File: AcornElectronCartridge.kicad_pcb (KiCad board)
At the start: 2 copper layers, 84.9 x 62.5 mm, 8 parts, among them P11 CONN_01X08, P12 CONN_01X08, P13 CONN_01X06, P21 CONN_01X06, P22 CONN_01X08, P23 CONN_01X08

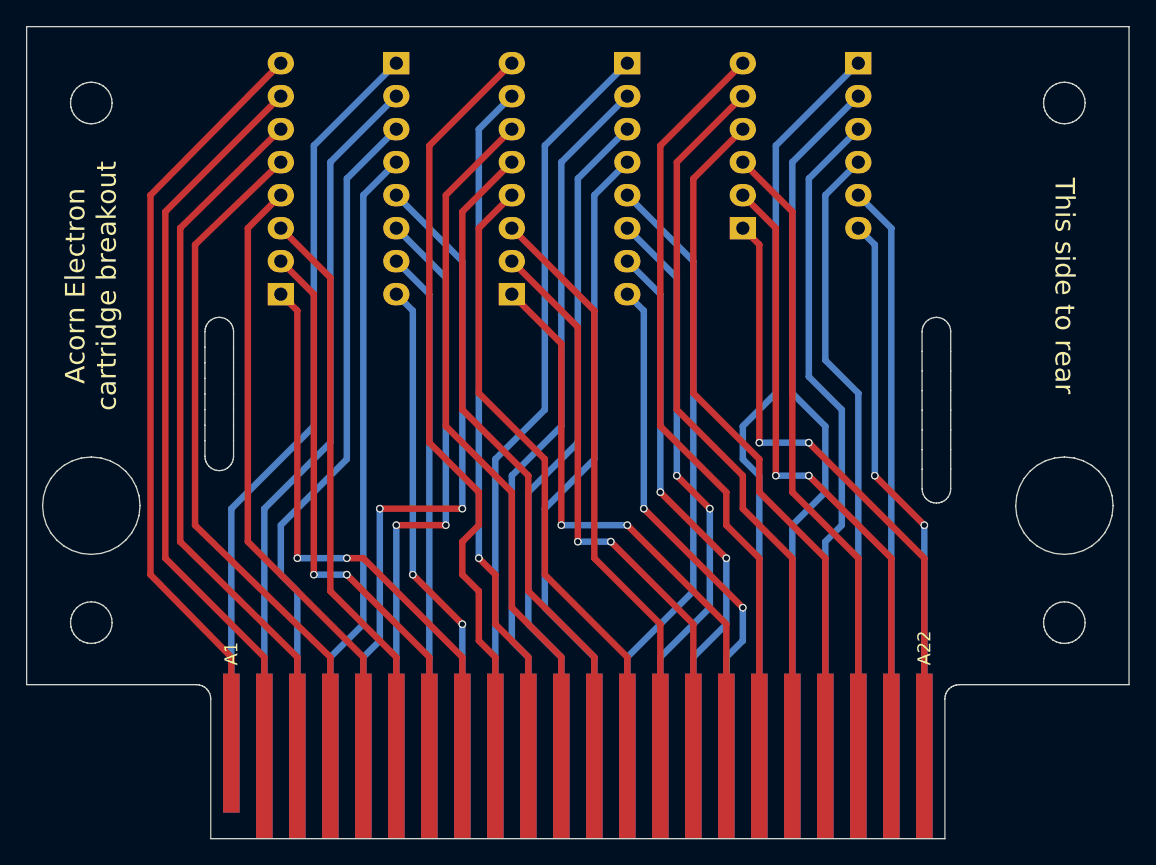
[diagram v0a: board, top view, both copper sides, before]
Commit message: Removed footprints, pads, vias and tracks. Changed labels to reflect the new use for the design.
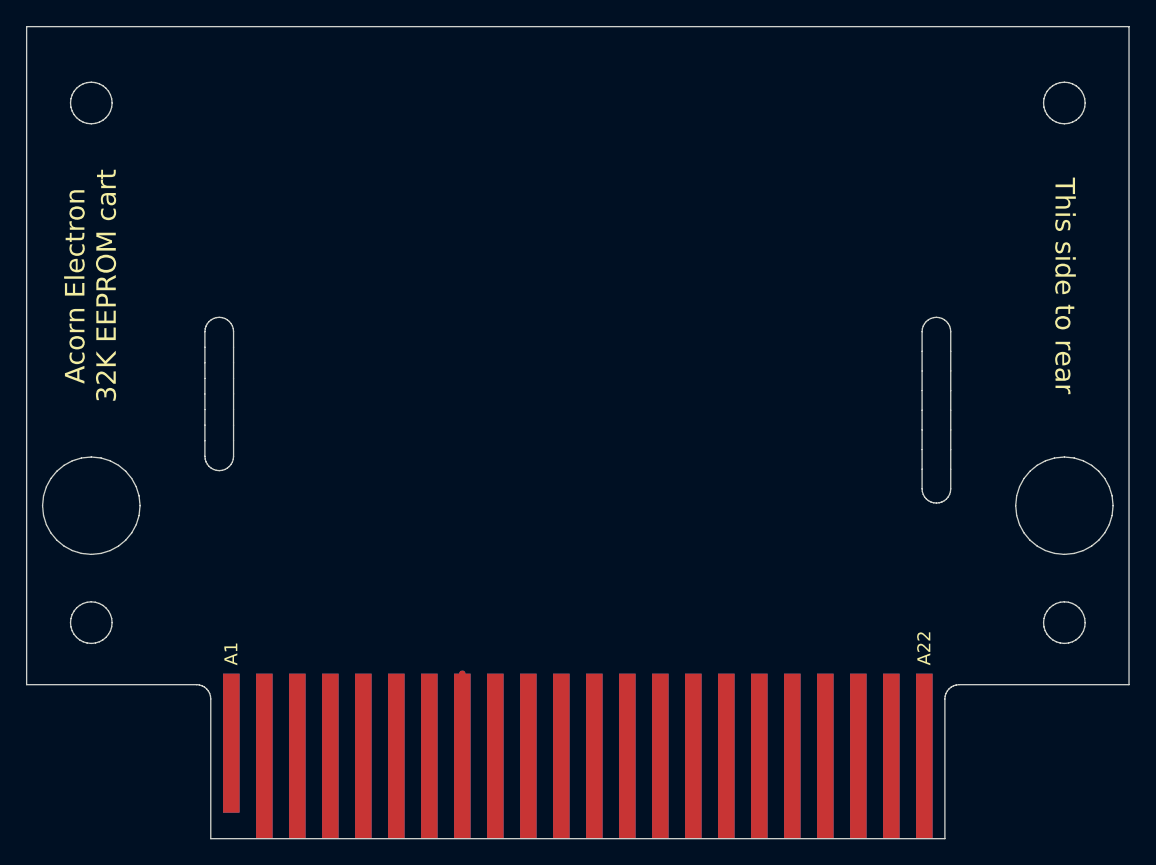
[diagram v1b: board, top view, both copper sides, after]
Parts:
- removed P11, P12, P22, P23: CONN_01X08, Pin_Headers:Pin_Header_Straight_1x08
- removed P13, P21: CONN_01X06, Pin_Headers:Pin_Header_Straight_1x06
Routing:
- net /+5V_A: track 60.0 -> 0.00 mm
- net /CLOCK: track 59.1 -> 0.00 mm
- net /-5V: track 59.1 -> 0.00 mm
- net /+5V_B: track 58.6 -> 0.00 mm
- net /nOE: track 57.6 -> 0.00 mm
- net /D4: track 57.5 -> 0.00 mm
- net /BA1: track 57.5 -> 0.00 mm
- net /nROMSTB: track 56.6 -> 0.00 mm
- net /nRST: track 55.3 -> 0.00 mm
- net /A10: track 55.0 -> 0.00 mm
- net /nOE2: track 55.0 -> 0.00 mm
- net /BA0: track 55.0 -> 0.00 mm
- net /READY: track 54.0 -> 0.00 mm
- net /ADOUT: track 54.0 -> 0.00 mm
- net /NC: track 53.4 -> 0.00 mm, vias 1 -> 0
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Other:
- board text added: "(C) 2017 David Boddie <david@boddie.org.uk> Design licensed under GPLv3 or later"
- board text added: "Acorn Electron 32K EEPROM cart"
- board text removed: "+5V"
- board text removed: "-5V"
- board text removed: "0V"
- board text removed: "A10"
- board text removed: "A11"
- board text removed: "A12"
- board text removed: "A13"
- board text removed: "A8"
- board text removed: "A9"
- board text removed: "ADIN"
- board text removed: "ADOUT"
- board text removed: "AGND"
- board text removed: "BA0"
- board text removed: "BA1"
- board text removed: "BA2"
- board text removed: "BA3"
- board text removed: "BA4"
- board text removed: "BA5"
- board text removed: "BA6"
- board text removed: "BA7"
- board text removed: "CLOCK"
- board text removed: "CSRW"
- board text removed: "Copyright (C) 2017 Paul Boddie <paul@boddie.org.uk> Design licensed under GPLv3 or later"
- board text removed: "D0"
- board text removed: "D1"
- board text removed: "D2"
- board text removed: "D3"
- board text removed: "D4"
- board text removed: "D5"
- board text removed: "D6"
- board text removed: "D7"
- board text removed: "NC"
- board text removed: "PHI2"
- board text removed: "READY"
- board text removed: "ROMQA"
- board text removed: "nINFC"
- board text removed: "nINFD"
- board text removed: "nIRQ"
- board text removed: "nNMI"
- board text removed: "nOE"
- board text removed: "nOE2"
- board text removed: "nROMSTB"
- board text removed: "nRST"

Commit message: Finished the basic design.
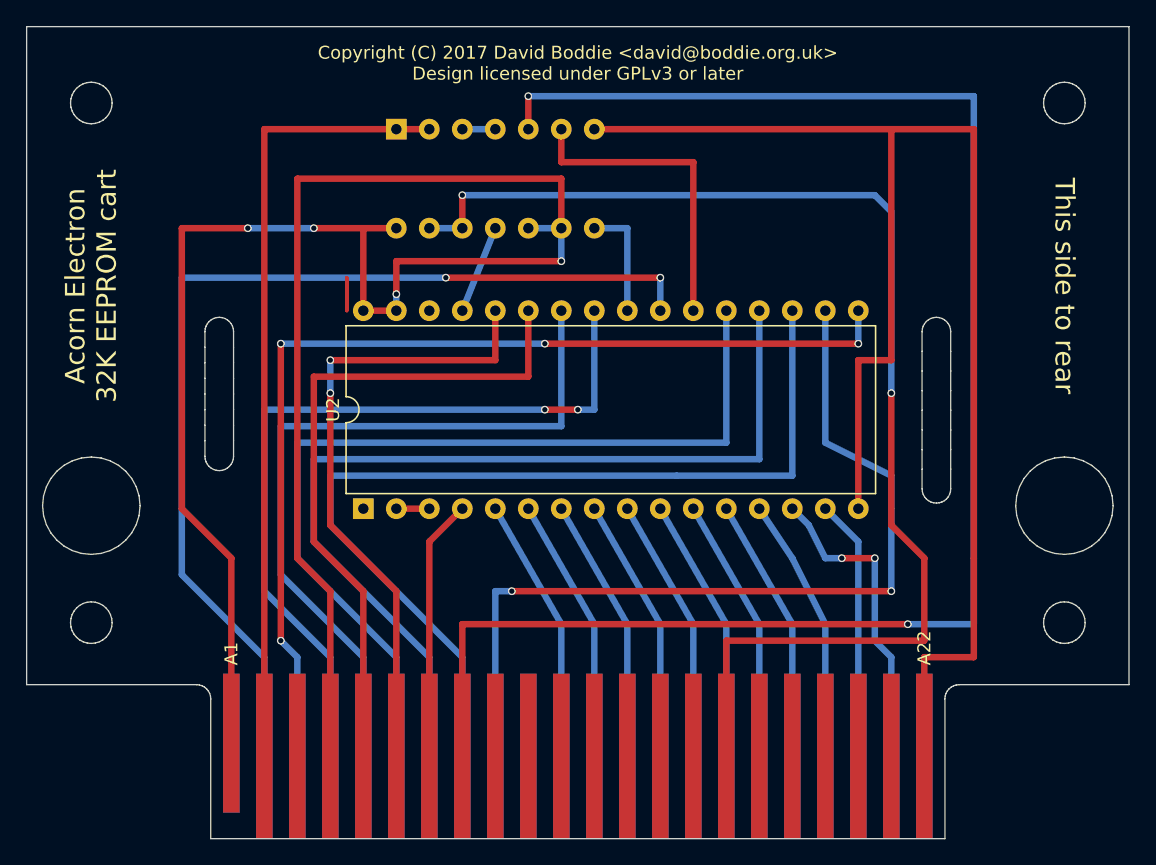
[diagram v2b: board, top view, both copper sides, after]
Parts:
- added U1: 74HC00, Housings_DIP:DIP-14_W7.62mm, B.Cu at (88.9, 72.4)
- added U2: SST39SF010, Housings_DIP:DIP-32_W15.24mm, F.Cu at (86.4, 101.6)
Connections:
- CONN1 pad 1: /+5V_A -> VCC
- CONN1 pad 22: /0V_A -> GND
- CONN2 pad 22: /0V_B -> GND
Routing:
- net /PHI2: track 6.35 -> 127.0 mm, vias 0 -> 2
- net GND: track 0.00 -> 115.6 mm
- net /ROMQA: track 0.00 -> 96.8 mm, vias 0 -> 2
- net /CSRW: track 0.00 -> 91.2 mm, vias 0 -> 2
- net /D3: track 0.00 -> 79.3 mm, vias 0 -> 4
- net /A10: track 0.00 -> 78.8 mm, vias 0 -> 2
- net /D5: track 0.00 -> 74.1 mm
- net /D6: track 0.00 -> 72.3 mm
- net /D7: track 0.00 -> 70.5 mm
- net /D4: track 0.00 -> 67.9 mm, vias 0 -> 2
- net VCC: track 0.00 -> 66.6 mm, vias 0 -> 2
- net /A11: track 0.00 -> 61.8 mm, vias 0 -> 2
- net /nOE: track 0.00 -> 61.0 mm
- net /A9: track 0.00 -> 58.5 mm
- net /A8: track 0.00 -> 52.4 mm
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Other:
- board text added: "Copyright (C) 2017 David Boddie <david@boddie.org.uk> Design licensed under GPLv3 or later"
- board text added: "F.Cu (front copper) layer is rear side of cartridge board. B.Cu (back copper) layer is front side of cartridge board. 74HC00 is attached to the front side of the board. Flash ROM is attached to the rear side."
- board text removed: "(C) 2017 David Boddie <david@boddie.org.uk> Design licensed under GPLv3 or later"
- board text removed: "F.Cu (front copper) layer is rear side of cartridge board. B.Cu (back copper) layer is front side of cartridge board. For prototyping, headers are attached to front side of board, not rear side as would be usual."

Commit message: Renamed components. Tidied up a little.
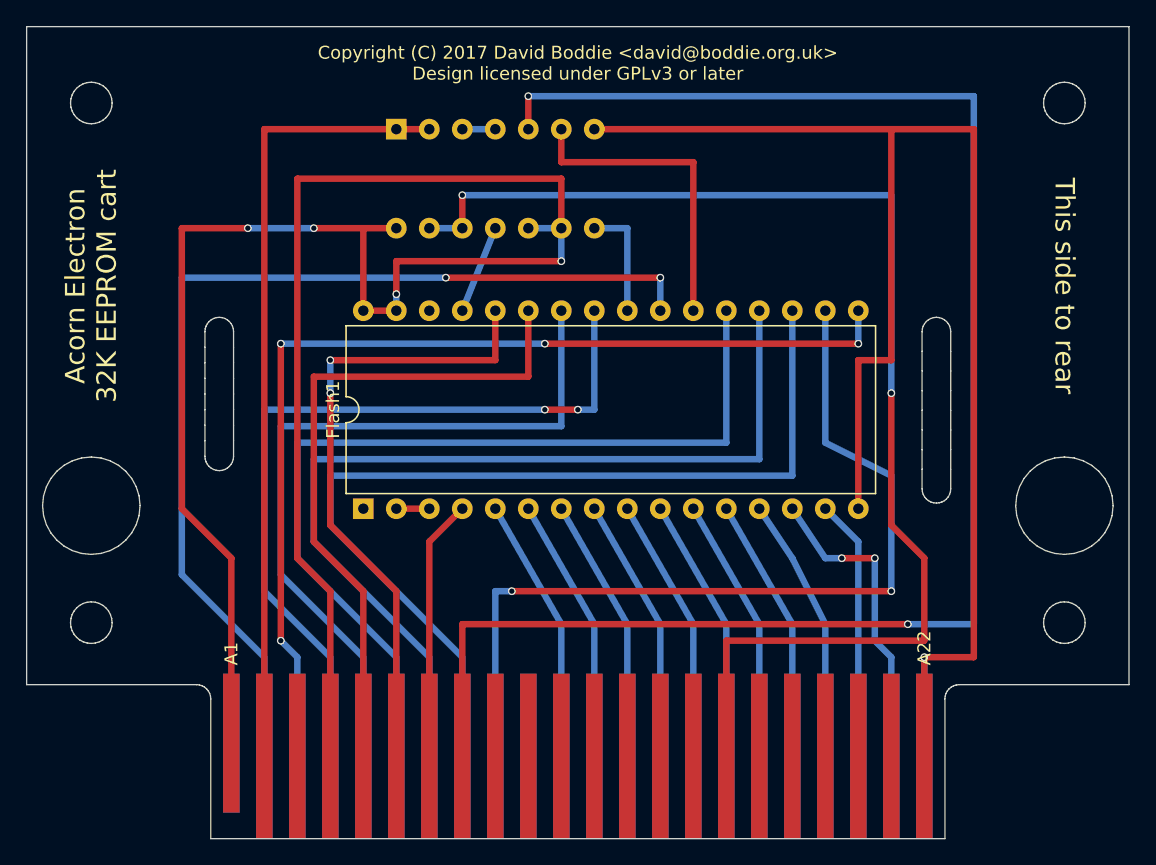
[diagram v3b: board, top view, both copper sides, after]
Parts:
- renumbered U2 to Flash1, U1 to NAND1
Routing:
- net (no net): track 7.62 -> 0.00 mm
- net GND: track 115.6 -> 123.2 mm, vias 0 -> 1
- net /ROMQA: track 96.8 -> 97.6 mm

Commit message: More minor improvements.
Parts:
- added 0V1: CONN_01X02, Pin_Headers:Pin_Header_Straight_1x02_Pitch2.54mm, F.Cu at (96.5, 106.7)
- added 5V1: CONN_01X02, Pin_Headers:Pin_Header_Straight_1x02_Pitch2.54mm, F.Cu at (76.2, 104.1)
- added PADS1: CONN_01X02, Pin_Headers:Pin_Header_Straight_1x02_Pitch2.54mm, F.Cu at (91.4, 106.7)
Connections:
- CONN2 pad 1: /+5V_B -> VCC
- Flash1 pad 2: GND -> /PAD0
- Flash1 pad 3: GND -> /PAD1
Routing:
- net GND: track 123.2 -> 153.7 mm
- net VCC: track 66.6 -> 75.0 mm, vias 2 -> 3
- net /PAD0: track 0.00 -> 6.88 mm
- net /PAD1: track 0.00 -> 2.54 mm
- net /D1: track 24.2 -> 23.4 mm
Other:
- board text added: "Acorn Electron Flash ROM cart"
- board text removed: "Acorn Electron 32K EEPROM cart"
- board text removed: "Acorn Electron cartridge breakout"

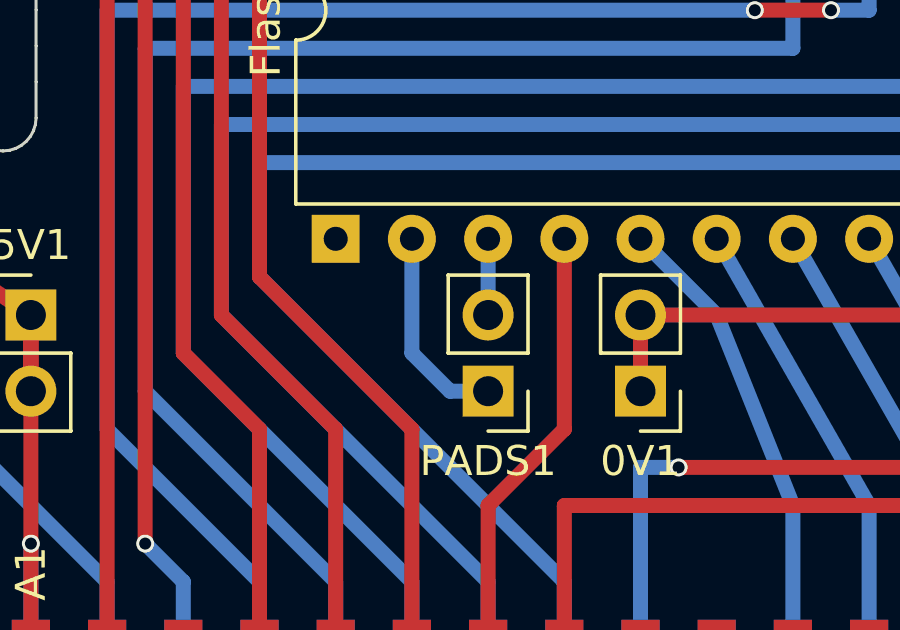
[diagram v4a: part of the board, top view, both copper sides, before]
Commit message: Moved two tracks to the other side of the board for clarity.
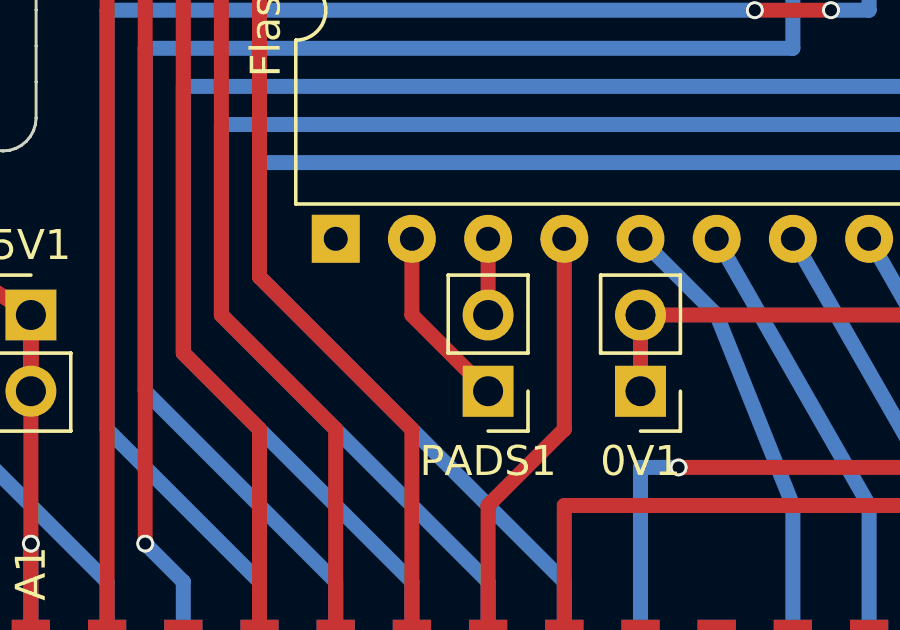
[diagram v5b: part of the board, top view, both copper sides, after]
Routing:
- net /PAD0: track 6.88 -> 6.13 mm
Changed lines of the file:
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@@
     (thickness 1.6)
     (drawings 322)
-    (tracks 178)
+    (tracks 177)
     (zones 0)
     (modules 7)
@@
   (segment (start 101.6 74.93) (end 101.6 72.39) (width 0.5) (layer F.Cu) (net 46) (status 20))
   (segment (start 111.76 74.93) (end 101.6 74.93) (width 0.5) (layer F.Cu) (net 46))
-  (segment (start 91.44 101.6) (end 91.44 104.14) (width 0.5) (layer B.Cu) (net 49))
-  (segment (start 88.9 101.6) (end 88.9 105.41) (width 0.5) (layer B.Cu) (net 50))
-  (segment (start 90.17 106.68) (end 91.44 106.68) (width 0.5) (layer B.Cu) (net 50))
-  (segment (start 88.9 105.41) (end 90.17 106.68) (width 0.5) (layer B.Cu) (net 50))
+  (segment (start 91.44 101.6) (end 91.44 104.14) (width 0.5) (layer F.Cu) (net 49) (status C00000))
+  (segment (start 88.9 101.6) (end 88.9 104.14) (width 0.5) (layer F.Cu) (net 50) (status 400000))
+  (segment (start 88.9 104.14) (end 91.44 106.68) (width 0.5) (layer F.Cu) (net 50) (status 800000))
   (zone (net 0) (net_name "") (layer F.Cu) (hatch edge 0.508)
     (connect_pads (clearance 0.508))

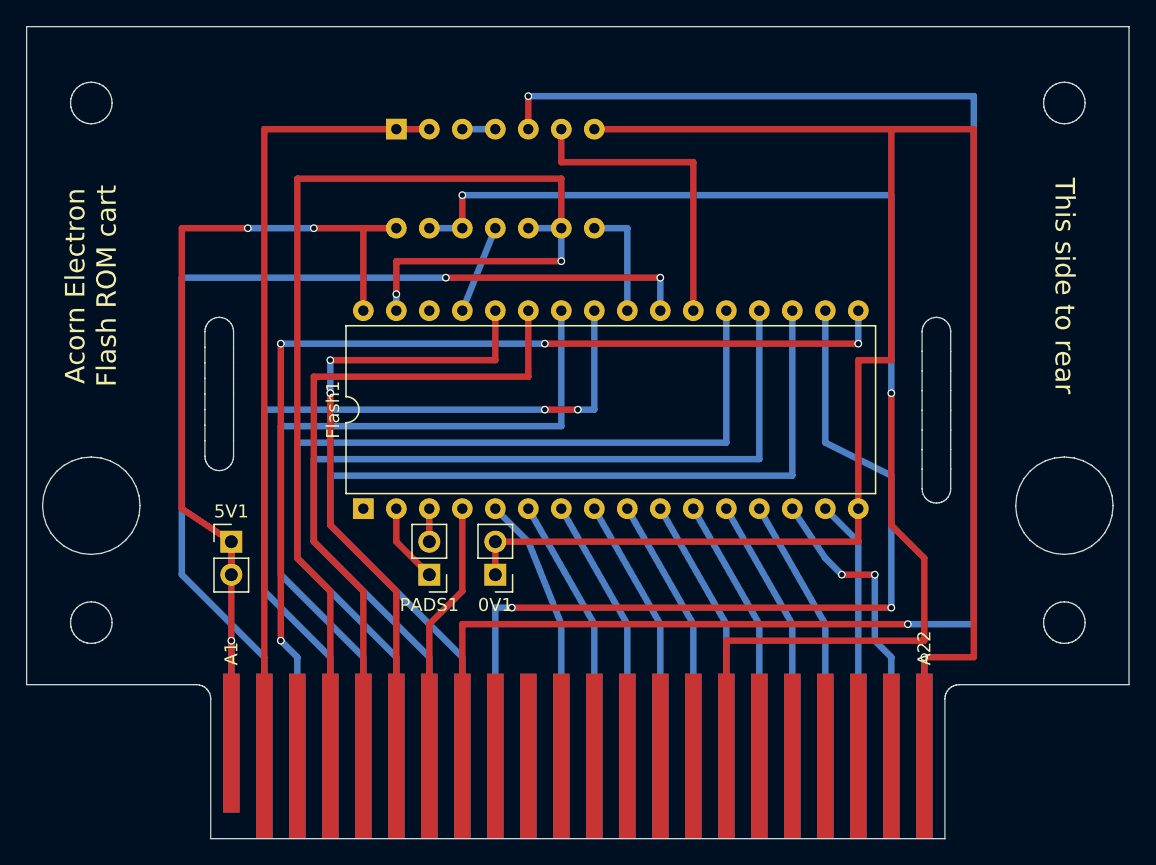
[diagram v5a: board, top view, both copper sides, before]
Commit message: Removed the pads and added flip-flops to support the use of the FC73 paging register for software-enabled bank selection.
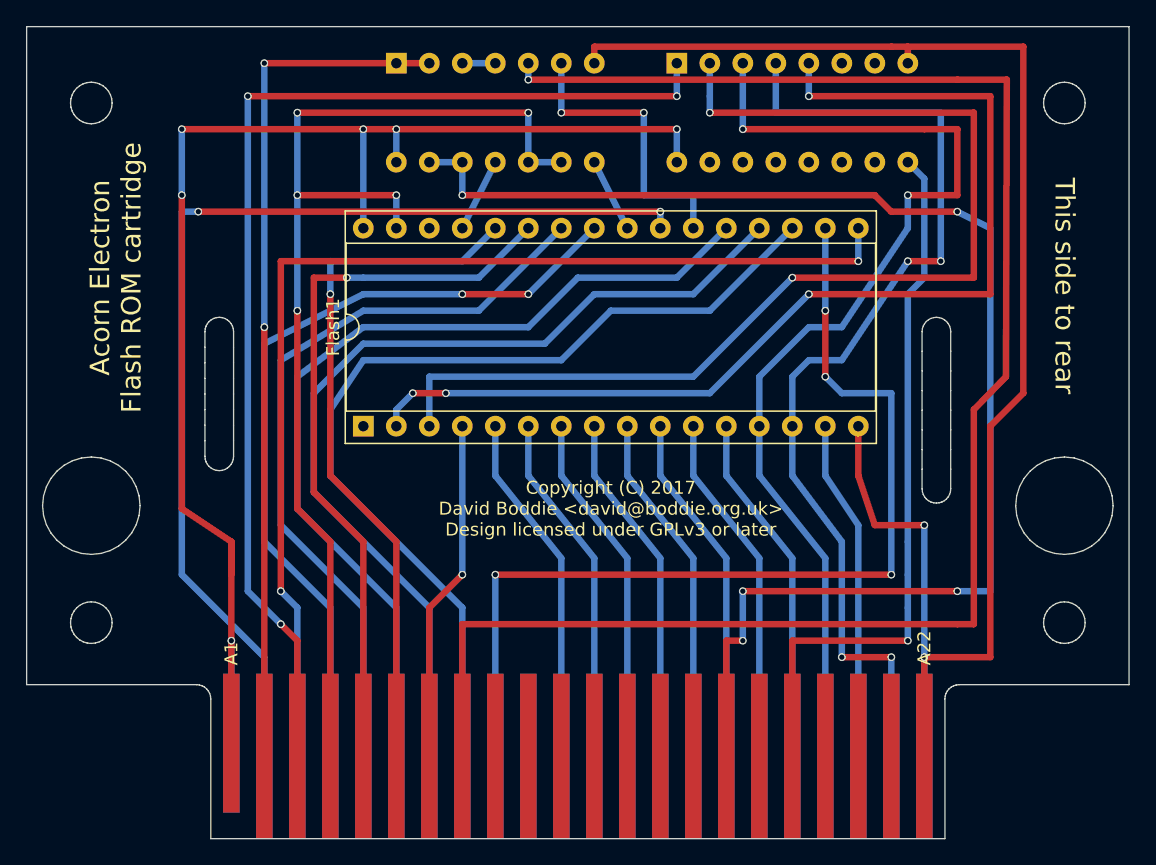
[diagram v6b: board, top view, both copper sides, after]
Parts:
- removed 0V1, 5V1, PADS1: CONN_01X02, Pin_Headers:Pin_Header_Straight_1x02_Pitch2.54mm
- added FLIP1: 74LS174, Housings_DIP:DIP-16_W7.62mm_Socket, B.Cu at (110.5, 67.3)
- Flash1: footprint Housings_DIP:DIP-32_W15.24mm -> Housings_DIP:DIP-32_W15.24mm_Socket
- NAND1: footprint Housings_DIP:DIP-14_W7.62mm -> Housings_DIP:DIP-14_W7.62mm_Socket
- moved Flash1 6.35 mm to (86.4, 95.2)
- moved NAND1 5.08 mm to (88.9, 67.3)
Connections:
- Flash1 pad 2: /PAD0 -> /A16
- Flash1 pad 3: /PAD1 -> /A15
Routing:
- net /nRST: track 0.00 -> 87.9 mm, vias 0 -> 3
- net /A15: track 0.00 -> 85.7 mm, vias 0 -> 2
- net /A16: track 0.00 -> 82.4 mm, vias 0 -> 4
- net /D0: track 20.4 -> 81.1 mm, vias 0 -> 2
- net /nROMSTB: track 0.00 -> 55.7 mm, vias 0 -> 1
- net /D1: track 23.4 -> 78.3 mm, vias 2 -> 4
- net VCC: track 75.0 -> 110.5 mm, vias 3 -> 6
- net GND: track 153.7 -> 125.7 mm, vias 1 -> 2
- net /ROMQA: track 97.6 -> 107.5 mm, vias 2 -> 5
- net /D4: track 67.9 -> 75.5 mm, vias 2 -> 4
- net /BA6: track 20.4 -> 27.2 mm
- net /BA4: track 20.4 -> 27.2 mm
- net /BA3: track 20.4 -> 27.2 mm
- net /BA2: track 20.4 -> 27.2 mm
- net /BA1: track 20.4 -> 27.2 mm
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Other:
- board text added: "Acorn Electron Flash ROM cartridge"
- board text removed: "Acorn Electron Flash ROM cart"
